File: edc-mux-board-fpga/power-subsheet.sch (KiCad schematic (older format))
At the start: 1 part, among them U1 10CL040YF484I7G

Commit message: starting to work on mezzanine board interconnections.
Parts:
- added FB?: 600Ω @ 100MHz, Capacitor_SMD:C_0805_2012Metric, symbol Device:Ferrite_Bead_Small
- added U?: 10CL040YF484I7G, SW-Intel:FBGA-484_23.0x23.0mm_Layout22x22_P1.0mm, symbol SW-Intel:10CL040YF484I7G
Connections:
- net +3V3: now also U?.A2 (VCCIO8), U?.A21 (VCCIO7), U?.AA6 (VCCIO3), U?.AB2 (VCCIO3), U?.AB21 (VCCIO4), U?.D11 (VCCIO8), U?.D12 (VCCIO7), U?.D14 (VCCIO7), U?.D16 (VCCIO7), U?.D18 (VCCIO7), U?.D4 (VCCIO1), U?.D5 (VCCIO8), U?.D9 (VCCIO8), U?.E19 (VCCIO6), U?.E8 (VCCIO8), U?.F4 (VCCIO1), U?.G19 (VCCIO6), U?.H4 (VCCIO1), U?.J20 (VCCIO6), U?.K4 (VCCIO1), U?.L19 (VCCIO6), U?.N4 (VCCIO2), U?.P18 (VCCIO5), U?.R4 (VCCIO2), U?.T19 (VCCIO5), U?.U4 (VCCIO2), U?.V19 (VCCIO5), U?.W11 (VCCIO3), U?.W12 (VCCIO4), U?.W16 (VCCIO4), U?.W18 (VCCIO4), U?.W4 (VCCIO2), U?.W5 (VCCIO3), U?.W9 (VCCIO3), U?.Y14 (VCCIO4), U?.Y19 (VCCIO5)
- net at U1.E17 (VCCD_PLL2), U1.F6 (VCCD_PLL3), U1.U6 (VCCD_PLL1)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: now also FB?.2
- net +2V5: now reaches U1.F18 (VCCA2), U1.G6 (VCCA3), U1.T6 (VCCA1), U1.U18 (VCCA4)
- net +1V2: now reaches U1.G12 (VCCINT), U1.H9 (VCCINT), U1.J10 (VCCINT), U1.J11 (VCCINT), U1.J12 (VCCINT), U1.J13 (VCCINT), U1.J14 (VCCINT), U1.J16 (VCCINT), U1.K14 (VCCINT), U1.K15 (VCCINT), U1.K9 (VCCINT), U1.L14 (VCCINT), U1.L16 (VCCINT), U1.L9 (VCCINT), U1.M14 (VCCINT), U1.M15 (VCCINT), U1.M9 (VCCINT), U1.N14 (VCCINT), U1.N9 (VCCINT), U1.P10 (VCCINT), U1.P11 (VCCINT), U1.P12 (VCCINT), U1.P13 (VCCINT), U1.P14 (VCCINT), U1.P9 (VCCINT), U1.R10 (VCCINT), U1.R12 (VCCINT), U1.R8 (VCCINT)
- net +1V2: now also FB?.1
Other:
- note added: "+12V net is main power supply for board. Produced from unregulated power input to board.\n+3V3 net is primary digital supply and IO voltage reference\n+1V8 net is digital supply\n+1V8A net is analog supply for CODECs. Connect to +1V8 using ferrite bead\n+1V2 net is internal core voltage for FGPA\n+2V5 net is FPGA PLL Analog Supply"
- note removed: "+12V net is main power supply for board. Produced from unregulated power input to board.\n+3V3 net is primary digital supply and IO voltage reference\n+1V8 net is digital supply\n+1V8A net is analog supply for CODECs. Connect to +1V8 using ferrite bead"
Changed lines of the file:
@@
 $Descr A4 11693 8268
 encoding utf-8
-Sheet 2 25
+Sheet 2 28
 Title ""
 Date ""
@@
 $EndComp
 Text Notes 6800 3550 0    50   ~ 0
-+12V net is main power supply for board. Produced from unregulated power input to board.\n+3V3 net is primary digital supply and IO voltage reference\n+1V8 net is digital supply\n+1V8A net is analog supply for CODECs. Connect to +1V8 using ferrite bead
++12V net is main power supply for board. Produced from unregulated power input to board.\n+3V3 net is primary digital supply and IO voltage reference\n+1V8 net is digital supply\n+1V8A net is analog supply for CODECs. Connect to +1V8 using ferrite bead\n+1V2 net is internal core voltage for FGPA\n+2V5 net is FPGA PLL Analog Supply
 $Comp
 L power:+12V #PWR01
@@
 	1    0    0    -1
 $EndComp
+$Comp
+L SW-Intel:10CL040YF484I7G U?
+U 2 1 5CB65921
+P 5000 4750
+F 0 "U?" H 5700 3550 50  0000 C CNN
+F 1 "10CL040YF484I7G" H 4600 5950 50  0000 C CNN
+F 2 "SW-Intel:FBGA-484_23.0x23.0mm_Layout22x22_P1.0mm" H 7700 5650 50  0001 C CNN
+F 3 "https://www.intel.com/content/www/us/en/programmable/products/fpga/cyclone-series/cyclone-10/cyclone-10-lp/support.html" H 7700 5650 50  0001 C CNN
+	2    5000 4750
+	1    0    0    -1
+$EndComp
+$Comp
+L power:+1V2 #PWR?
+U 1 1 5CB73B8B
+P 5200 1750
+F 0 "#PWR?" H 5200 1600 50  0001 C CNN
+F 1 "+1V2" H 5200 1890 50  0000 C CNN
+F 2 "" H 5200 1750 50  0001 C CNN
+F 3 "" H 5200 1750 50  0001 C CNN
+	1    5200 1750
+	1    0    0    -1
+$EndComp
+$Comp
+L power:+2V5 #PWR?
+U 1 1 5CB747E3
+P 4900 1750
+F 0 "#PWR?" H 4900 1600 50  0001 C CNN
+F 1 "+2V5" H 4900 1890 50  0000 C CNN
+F 2 "" H 4900 1750 50  0001 C CNN
+F 3 "" H 4900 1750 50  0001 C CNN
+	1    4900 1750
+	1    0    0    -1
+$EndComp
+Wire Wire Line
+	5200 1750 5200 2050
+Wire Wire Line
+	5200 2050 5300 2050
+Wire Wire Line
+	4900 1750 4900 2450
+Wire Wire Line
+	4900 2450 5450 2450
+$Comp
+L Device:Ferrite_Bead_Small FB?
+U 1 1 5CB7D07D
+P 5300 2150
+AR Path="/5CC6CC1A/5CC6D47B/5CB7D07D" Ref="FB?"  Part="1"
+AR Path="/5CC3E5DC/5CB7D07D" Ref="FB?"  Part="1"
+AR Path="/5CC3E5B8/5CB7D07D" Ref="FB?"  Part="1"
+F 0 "FB?" H 5200 2200 50  0000 R CNN
+F 1 "600Ω @ 100MHz" H 5200 2150 50  0000 R CNN
+F 2 "Capacitor_SMD:C_0805_2012Metric" V 5230 2150 50  0001 C CNN
+F 3 "~" H 5300 2150 50  0001 C CNN
+F 4 "Murata" H 5300 2150 50  0001 C CNN "Manufacturer"
+F 5 "0805in/2012mm" H 5300 2150 50  0001 C CNN "Package ID"
+F 6 "BLM21AG601BH1" H 5300 2150 50  0001 C CNN "Manufacturers Part Number"
+	1    5300 2150
+	1    0    0    -1
+$EndComp
+Wire Wire Line
+	5450 2250 5300 2250
+Connection ~ 5300 2050
+Wire Wire Line
+	5300 2050 5450 2050
+$Comp
+L power:+3V3 #PWR?
+U 1 1 5CB85315
+P 4450 4150
+F 0 "#PWR?" H 4450 4000 50  0001 C CNN
+F 1 "+3V3" H 4450 4290 50  0000 C CNN
+F 2 "" H 4450 4150 50  0001 C CNN
+F 3 "" H 4450 4150 50  0001 C CNN
+	1    4450 4150
+	1    0    0    -1
+$EndComp
+Wire Wire Line
+	4800 4400 4450 4400
+Wire Wire Line
+	4450 4400 4450 4150
+Wire Wire Line
+	4800 4500 4450 4500
+Wire Wire Line
+	4450 4500 4450 4400
+Connection ~ 4450 4400
+Wire Wire Line
+	4800 4600 4450 4600
+Wire Wire Line
+	4450 4600 4450 4500
+Connection ~ 4450 4500
+Wire Wire Line
+	4800 4700 4450 4700
+Wire Wire Line
+	4450 4700 4450 4600
+Connection ~ 4450 4600
+Wire Wire Line
+	4800 4800 4450 4800
+Wire Wire Line
+	4450 4800 4450 4700
+Connection ~ 4450 4700
+Wire Wire Line
+	4800 4900 4450 4900
+Wire Wire Line
+	4450 4900 4450 4800
+Connection ~ 4450 4800
+Wire Wire Line
+	4800 5000 4450 5000
+Wire Wire Line
+	4450 5000 4450 4900
+Connection ~ 4450 4900
+Wire Wire Line
+	4800 5100 4450 5100
+Wire Wire Line
+	4450 5100 4450 5000
+Connection ~ 4450 5000
 $EndSCHEMATC

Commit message: unannotated components after major changes
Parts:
- renumbered U1 to U?
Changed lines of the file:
@@
 $EndDescr
 $Comp
-L SW-Intel:10CL040YF484I7G U1
+L SW-Intel:10CL040YF484I7G U?
 U 1 1 5CB1DD91
 P 6050 2250
-F 0 "U1" H 6050 2850 50  0000 C CNN
+F 0 "U?" H 6050 2850 50  0000 C CNN
 F 1 "10CL040YF484I7G" H 6050 2750 50  0000 C CNN
 F 2 "SW-Intel:FBGA-484_23.0x23.0mm_Layout22x22_P1.0mm" H 8750 3150 50  0001 C CNN
@@
 $EndComp
 $Comp
-L power:+3V3 #PWR02
+L power:+3V3 #PWR?
 U 1 1 5CC2D266
 P 7700 3050
-F 0 "#PWR02" H 7700 2900 50  0001 C CNN
+F 0 "#PWR?" H 7700 2900 50  0001 C CNN
 F 1 "+3V3" H 7700 3190 50  0000 C CNN
 F 2 "" H 7700 3050 50  0001 C CNN
@@
 $EndComp
 $Comp
-L power:+1V8 #PWR03
+L power:+1V8 #PWR?
 U 1 1 5CC2D9F8
 P 8050 3200
-F 0 "#PWR03" H 8050 3050 50  0001 C CNN
+F 0 "#PWR?" H 8050 3050 50  0001 C CNN
 F 1 "+1V8" H 8050 3340 50  0000 C CNN
 F 2 "" H 8050 3200 50  0001 C CNN
@@
 $EndComp
 $Comp
-L SW-power:+1V8A #+1V8A01
+L SW-power:+1V8A #+1V8A?
 U 1 1 5CC2E124
 P 8550 3200
-F 0 "#+1V8A01" H 9300 2900 60  0001 C CNN
+F 0 "#+1V8A?" H 9300 2900 60  0001 C CNN
 F 1 "+1V8A" H 8550 3350 50  0000 C CNN
 F 2 "" H 8550 3200 60  0001 C CNN
@@
 $EndComp
 $Comp
-L power:GND #PWR04
+L power:GND #PWR?
 U 1 1 5CC2E87F
 P 8100 3800
-F 0 "#PWR04" H 8100 3550 50  0001 C CNN
+F 0 "#PWR?" H 8100 3550 50  0001 C CNN
 F 1 "GND" H 8100 3650 50  0000 C CNN
 F 2 "" H 8100 3800 50  0001 C CNN
@@
 +12V net is main power supply for board. Produced from unregulated power input to board.\n+3V3 net is primary digital supply and IO voltage reference\n+1V8 net is digital supply\n+1V8A net is analog supply for CODECs. Connect to +1V8 using ferrite bead\n+1V2 net is internal core voltage for FGPA\n+2V5 net is FPGA PLL Analog Supply
 $Comp
-L power:+12V #PWR01
+L power:+12V #PWR?
 U 1 1 5CC7BE37
 P 7400 3000
-F 0 "#PWR01" H 7400 2850 50  0001 C CNN
+F 0 "#PWR?" H 7400 2850 50  0001 C CNN
 F 1 "+12V" H 7400 3140 50  0000 C CNN
 F 2 "" H 7400 3000 50  0001 C CNN

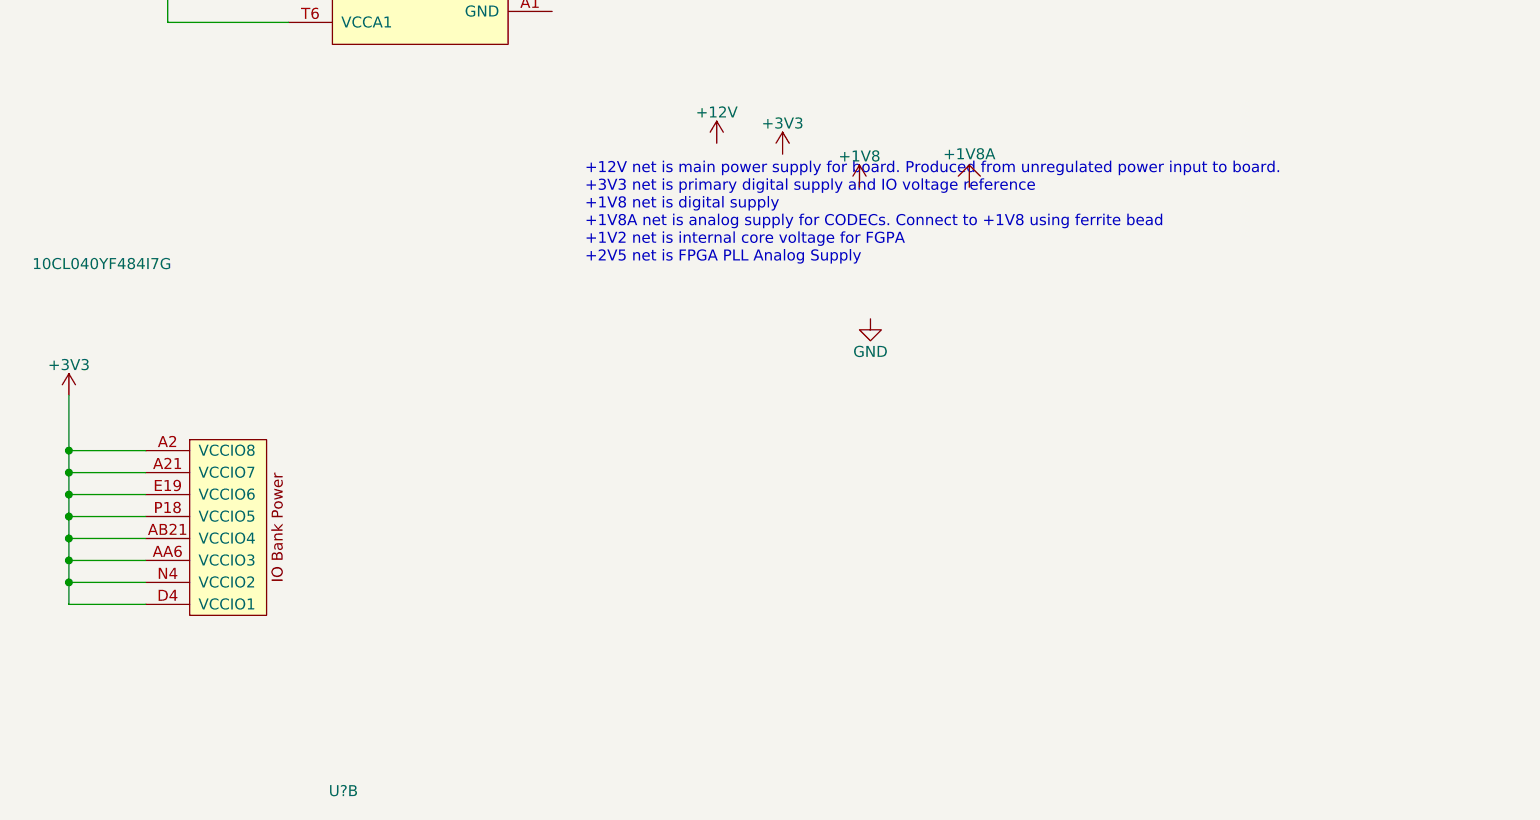
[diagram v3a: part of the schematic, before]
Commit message: finished draft of horizontal pcb connector pinout.
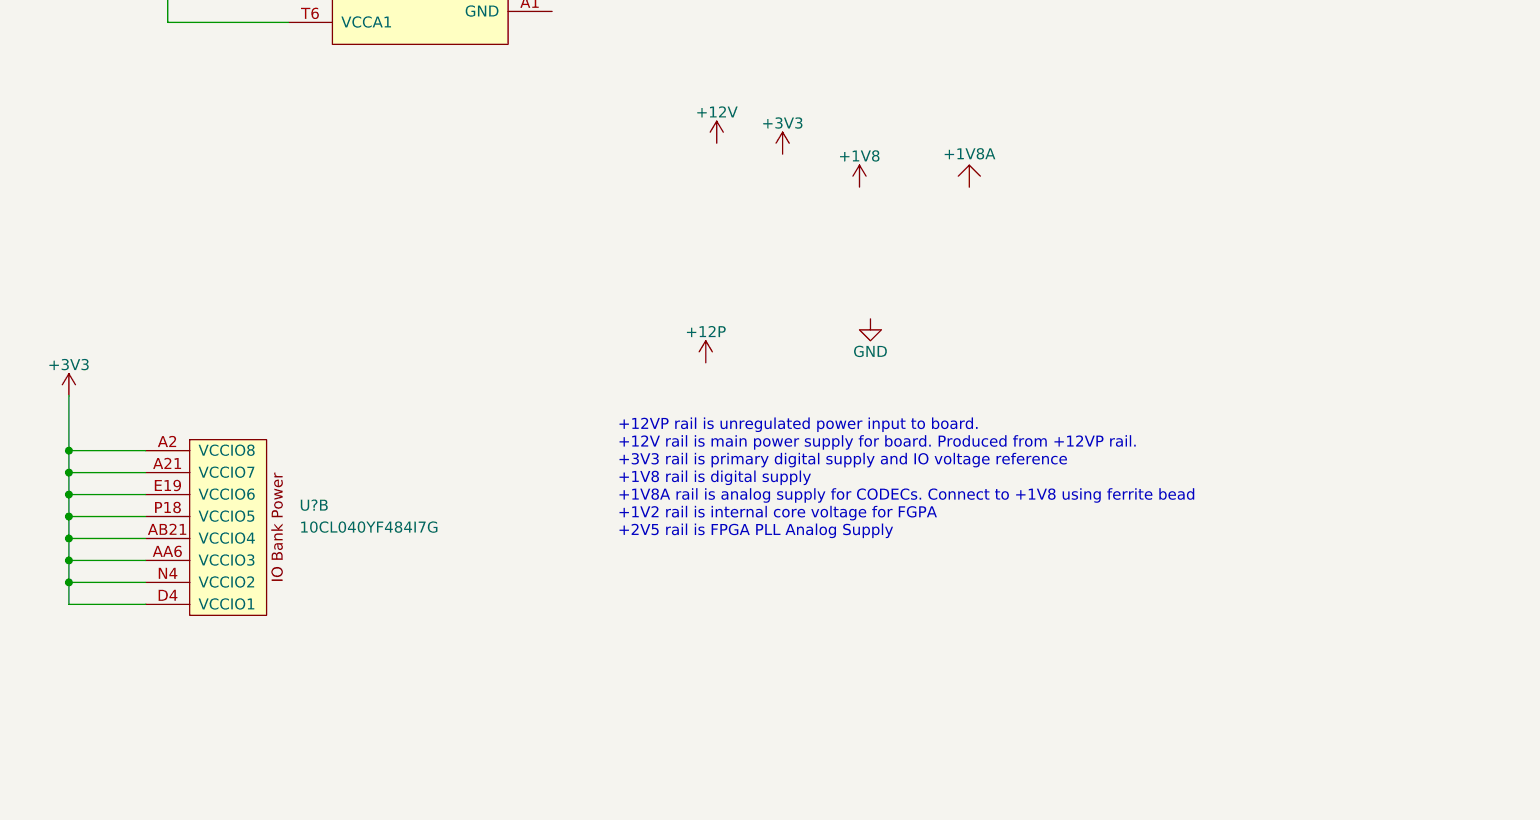
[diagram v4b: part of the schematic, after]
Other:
- note added: "+12VP rail is unregulated power input to board.\n+12V rail is main power supply for board. Produced from +12VP rail.\n+3V3 rail is primary digital supply and IO voltage reference\n+1V8 rail is digital supply\n+1V8A rail is analog supply for CODECs. Connect to +1V8 using ferrite bead\n+1V2 rail is internal core voltage for FGPA\n+2V5 rail is FPGA PLL Analog Supply"
- note removed: "+12V net is main power supply for board. Produced from unregulated power input to board.\n+3V3 net is primary digital supply and IO voltage reference\n+1V8 net is digital supply\n+1V8A net is analog supply for CODECs. Connect to +1V8 using ferrite bead\n+1V2 net is internal core voltage for FGPA\n+2V5 net is FPGA PLL Analog Supply"
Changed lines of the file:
@@
 	1    0    0    -1
 $EndComp
-Text Notes 6800 3550 0    50   ~ 0
-+12V net is main power supply for board. Produced from unregulated power input to board.\n+3V3 net is primary digital supply and IO voltage reference\n+1V8 net is digital supply\n+1V8A net is analog supply for CODECs. Connect to +1V8 using ferrite bead\n+1V2 net is internal core voltage for FGPA\n+2V5 net is FPGA PLL Analog Supply
+Text Notes 6950 4800 0    50   ~ 0
++12VP rail is unregulated power input to board.\n+12V rail is main power supply for board. Produced from +12VP rail.\n+3V3 rail is primary digital supply and IO voltage reference\n+1V8 rail is digital supply\n+1V8A rail is analog supply for CODECs. Connect to +1V8 using ferrite bead\n+1V2 rail is internal core voltage for FGPA\n+2V5 rail is FPGA PLL Analog Supply
 $Comp
 L power:+12V #PWR?
@@
 U 2 1 5CB65921
 P 5000 4750
-F 0 "U?" H 5700 3550 50  0000 C CNN
-F 1 "10CL040YF484I7G" H 4600 5950 50  0000 C CNN
+F 0 "U?" H 5500 4850 50  0000 L CNN
+F 1 "10CL040YF484I7G" H 5500 4750 50  0000 L CNN
 F 2 "SW-Intel:FBGA-484_23.0x23.0mm_Layout22x22_P1.0mm" H 7700 5650 50  0001 C CNN
 F 3 "https://www.intel.com/content/www/us/en/programmable/products/fpga/cyclone-series/cyclone-10/cyclone-10-lp/support.html" H 7700 5650 50  0001 C CNN
@@
 	4450 5100 4450 5000
 Connection ~ 4450 5000
+$Comp
+L power:+12P #PWR?
+U 1 1 62666C46
+P 7350 4000
+F 0 "#PWR?" H 7350 3850 50  0001 C CNN
+F 1 "+12P" H 7350 4140 50  0000 C CNN
+F 2 "" H 7350 4000 50  0001 C CNN
+F 3 "" H 7350 4000 50  0001 C CNN
+	1    7350 4000
+	1    0    0    -1
+$EndComp
 $EndSCHEMATC

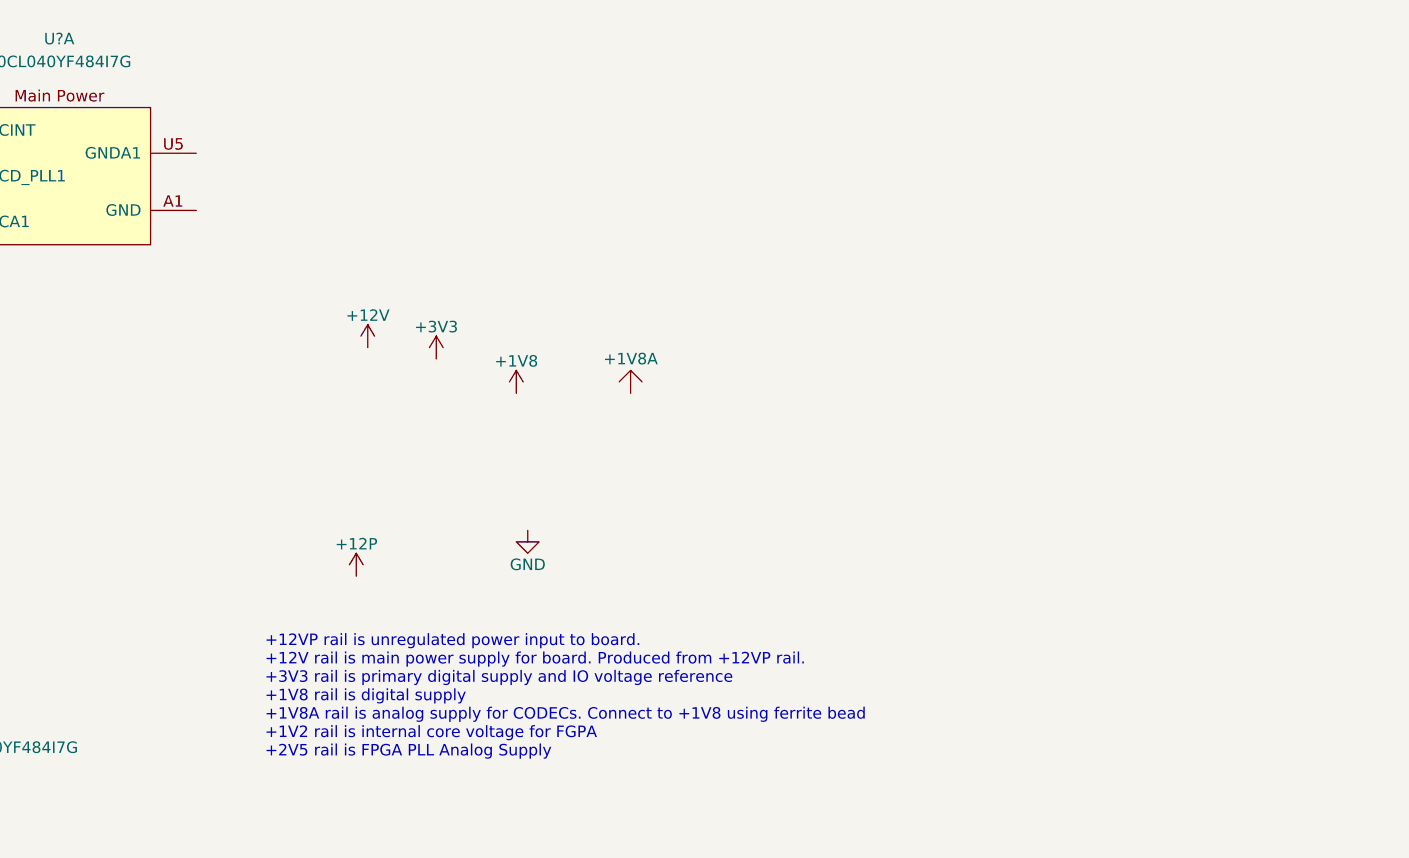
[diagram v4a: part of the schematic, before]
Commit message: added ground connections to fpga
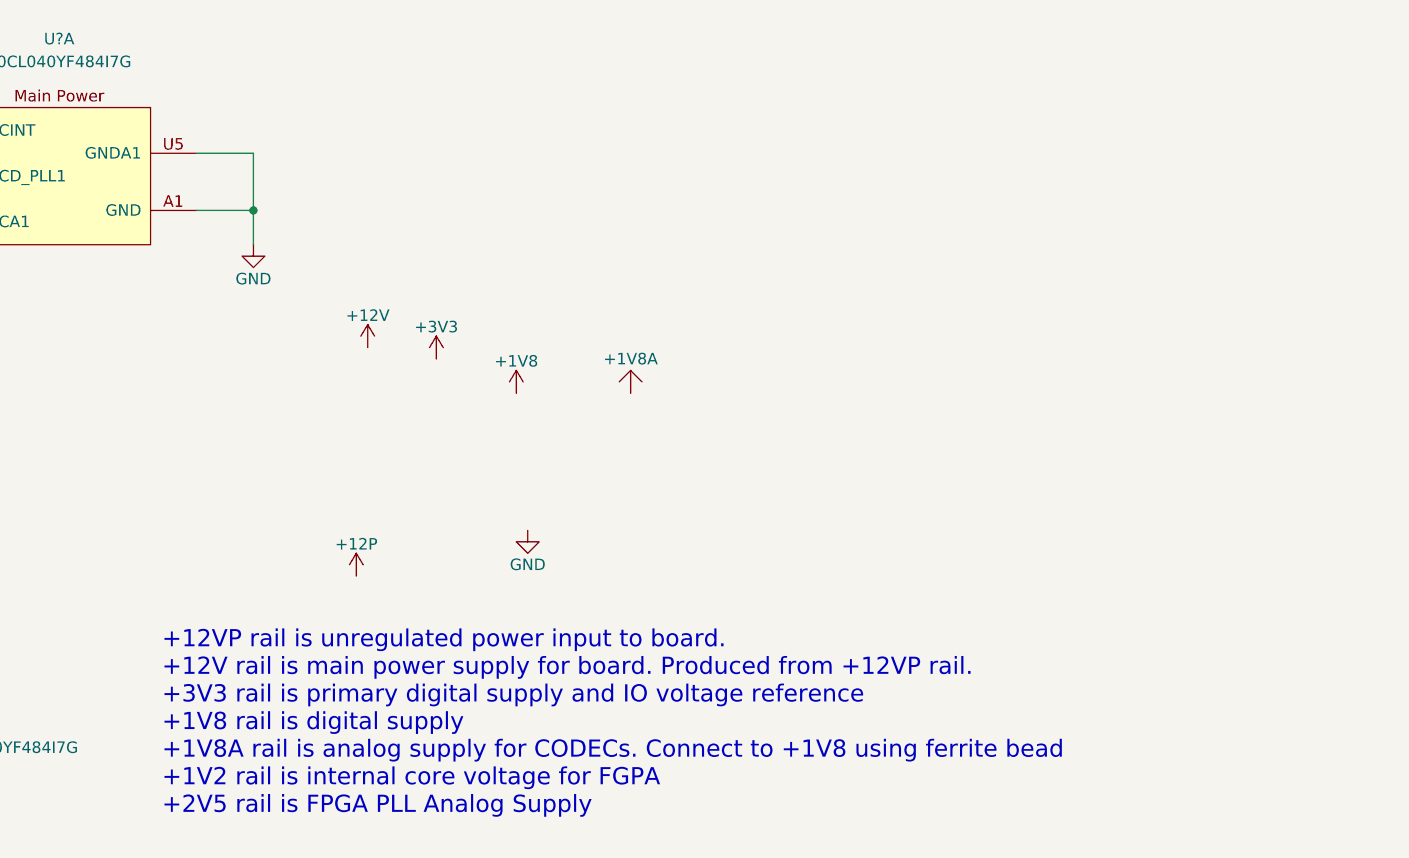
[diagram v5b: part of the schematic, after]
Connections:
- net GND: now also U?.A1 (GND), U?.A22 (GND), U?.AA1 (GND), U?.AA17 (GND), U?.AA2 (GND), U?.AB1 (GND), U?.AB17 (GND), U?.AB22 (GND), U?.AB6 (GND), U?.C1 (GND), U?.C11 (GND), U?.C12 (GND), U?.C14 (GND), U?.C16 (GND), U?.C18 (GND), U?.C2 (GND), U?.C5 (GND), U?.C9 (GND), U?.D3 (GND), U?.D8 (GND), U?.E18 (GNDA2), U?.E20 (GND), U?.F12 (GND), U?.F3 (GND), U?.F5 (GNDA3), U?.G20 (GND), U?.H12 (GND), U?.H13 (GND), U?.H3 (GND), U?.J15 (GND), U?.J19 (GND), U?.J9 (GND), U?.K10 (GND), U?.K11 (GND), U?.K12 (GND), U?.K13 (GND), U?.K16 (GND), U?.K3 (GND), U?.L10 (GND), U?.L11 (GND), U?.L12 (GND), U?.L13 (GND), U?.L15 (GND), U?.L20 (GND), U?.M10 (GND), U?.M11 (GND), U?.M12 (GND), U?.M13 (GND), U?.N10 (GND), U?.N11 (GND), U?.N12 (GND), U?.N13 (GND), U?.N15 (GND), U?.N3 (GND), U?.P19 (GND), U?.P8 (GND), U?.R11 (GND), U?.R13 (GND), U?.R3 (GND), U?.R9 (GND), U?.T20 (GND), U?.U3 (GND), U?.U5 (GNDA1), U?.V18 (GNDA4), U?.V20 (GND), U?.W3 (GND), U?.Y11 (GND), U?.Y12 (GND), U?.Y15 (GND), U?.Y16 (GND), U?.Y18 (GND), U?.Y20 (GND), U?.Y5 (GND), U?.Y9 (GND)
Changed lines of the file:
@@
 	1    0    0    -1
 $EndComp
-Text Notes 6950 4800 0    50   ~ 0
+Text Notes 6500 5050 0    75   ~ 0
 +12VP rail is unregulated power input to board.\n+12V rail is main power supply for board. Produced from +12VP rail.\n+3V3 rail is primary digital supply and IO voltage reference\n+1V8 rail is digital supply\n+1V8A rail is analog supply for CODECs. Connect to +1V8 using ferrite bead\n+1V2 rail is internal core voltage for FGPA\n+2V5 rail is FPGA PLL Analog Supply
 $Comp
@@
 	1    0    0    -1
 $EndComp
+$Comp
+L power:GND #PWR?
+U 1 1 6573E3B5
+P 6900 2550
+F 0 "#PWR?" H 6900 2300 50  0001 C CNN
+F 1 "GND" H 6900 2400 50  0000 C CNN
+F 2 "" H 6900 2550 50  0001 C CNN
+F 3 "" H 6900 2550 50  0001 C CNN
+	1    6900 2550
+	1    0    0    -1
+$EndComp
+Wire Wire Line
+	6650 2150 6900 2150
+Wire Wire Line
+	6900 2150 6900 2400
+Wire Wire Line
+	6650 2400 6900 2400
+Connection ~ 6900 2400
+Wire Wire Line
+	6900 2400 6900 2550
 $EndSCHEMATC
